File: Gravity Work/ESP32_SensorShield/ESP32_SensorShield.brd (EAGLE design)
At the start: 65.4 x 22.9 mm, 46 parts, among them IC1 BMP388, U1 FGPMMOPA6H, U2 MB85RC256VPF-G-JNERE2, U3 SPX3819-3.3, U4 SN65HVD230D, Y1 32.768kHz

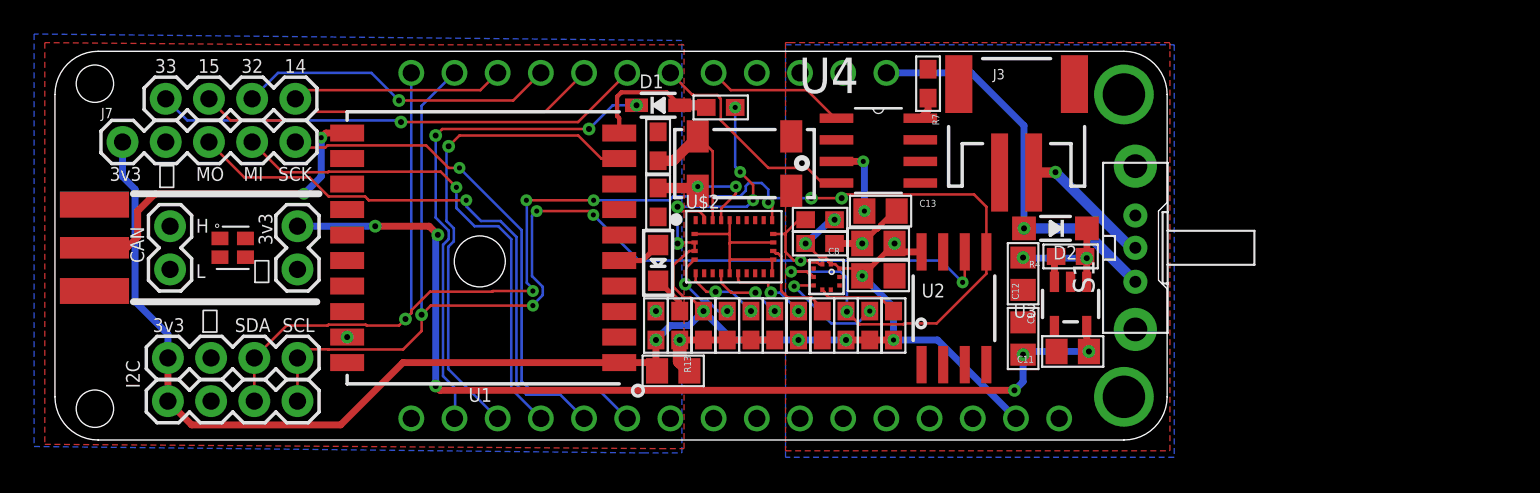
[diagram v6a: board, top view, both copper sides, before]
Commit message: Completed Routing and Fixed DRC Errors. Need to Perfrom Final Check w/ Butch and Selfcheck.
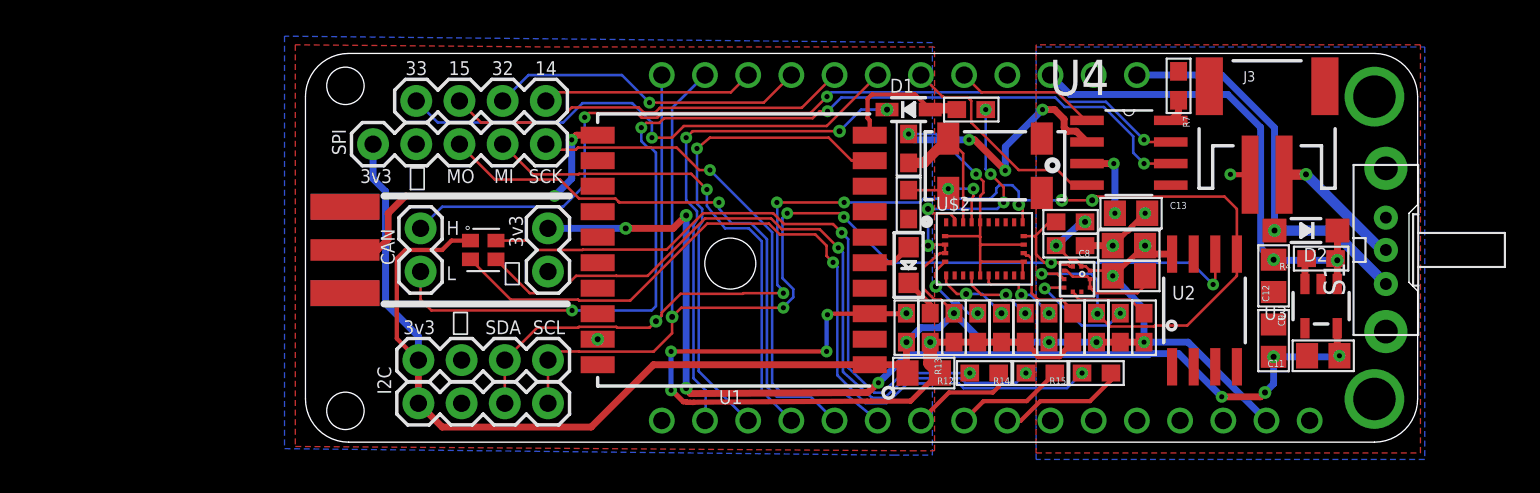
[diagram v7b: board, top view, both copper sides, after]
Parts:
- removed J1, J2, J8: (no value), SparkFun-Connectors:1X04
- removed J4, J6: (no value), SparkFun-Connectors:1X02
- removed J7: (no value), SparkFun-Connectors:1X05
- added AUX_3V3, CAN: (no value), SparkFun-Connectors:1X02
- added CS, I2C1, I2C2: (no value), SparkFun-Connectors:1X04
- added R12, R14, R15: 1k, microbuilder:0603
- added SPI: (no value), SparkFun-Connectors:1X05
- moved D1 14.7 mm to (35.6, 19.6)
- moved C11 14.7 mm to (59.9, 5.08)
- moved C12 14.7 mm to (57.0, 5.97)
- moved C8 14.7 mm to (48.5, 11.6)
- moved C9 14.7 mm to (57.0, 9.78)
- moved J3 14.7 mm to (56.6, 19.4)
- moved U2 14.7 mm to (53.0, 7.75)
- moved U4 14.7 mm to (48.5, 17.0)
- moved C1 14.7 mm to (35.6, 17.3)
- moved C2 14.7 mm to (35.6, 14.0)
- moved LED1 14.7 mm to (35.6, 10.4)
- moved R10 14.7 mm to (39.2, 19.6)
- moved R2 14.7 mm to (39.6, 6.73)
- moved R3 14.7 mm to (45.2, 6.73)
- moved R9 14.7 mm to (46.6, 6.73)
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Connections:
- new net LED_B: R12.1, U$1.10
- new net LED_G: R14.1, U$1.9
- new net LED_R: R15.1, U$1.8
- new net N$12: R12.2, U$36.BLUE
- new net N$13: R14.2, U$36.GREEN
- new net N$14: R15.2, U$36.RED
- net 3.3V: now also I2C1.1, I2C2.1, SPI.1, U$36.CA; no longer J1.1, J2.1, J7.1
- net AUX_3V3: now also AUX_3V3.2; no longer J4.2
- net CANH: now also CAN.2
- net CANL: now also CAN.1
- net GND: now also AUX_3V3.1, I2C1.2, I2C2.2, SPI.2; no longer J1.2, J2.2, J4.1, J7.2
- net GPIO14: now also CS.4; no longer J8.4
- net GPIO15: now also CS.2; no longer J8.2
- net GPIO32: now also CS.3; no longer J8.3
- net GPIO33: now also CS.1; no longer J8.1
- net MISO: now also SPI.4; no longer J7.4
- net MOSI: now also SPI.3; no longer J7.3
- net SCK: now also SPI.5; no longer J7.5
- net SCL: now also I2C1.4, I2C2.4; no longer J1.4, J2.4
- net SDA: now also I2C1.3, I2C2.3; no longer J1.3, J2.3
- net VUSB: now also U$1.19
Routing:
- net GND: track 23.3 -> 92.4 mm, vias 4 -> 15
- net CANL: track 0.00 -> 60.9 mm, vias 0 -> 4
- net CANH: track 0.00 -> 51.2 mm, vias 0 -> 3
- net N$14: track 0.00 -> 48.3 mm, vias 0 -> 2
- net N$13: track 0.00 -> 43.1 mm, vias 0 -> 2
- net N$12: track 0.00 -> 38.2 mm, vias 0 -> 2
- net VUSB: track 6.99 -> 28.8 mm
- net 3.3V: track 110.6 -> 121.7 mm
- net LED_R: track 0.00 -> 7.50 mm
- net LED_G: track 0.00 -> 6.49 mm
- net LED_B: track 0.00 -> 6.20 mm
- net AUX_3V3: track 59.4 -> 62.7 mm, vias 6 -> 8
- net GPIO33: track 28.9 -> 31.0 mm
- net N$2: track 6.97 -> 6.09 mm
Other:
- board text added: "SPI"

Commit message: Added CAN Resistor, GPS GND Line Connected, Fixed Decoup Cap Value for AUX 3V3, Fixed Switch to not extend board size
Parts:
- added R16: 120, microbuilder:0603
- C12: value 0.1uF -> 1uF
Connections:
- removed net GND1: X1.GND@4
- removed net GND2: X1.GND@3
- net CANH: now also R16.1
- net CANL: now also R16.2
- net GND: now also U1.P$12, X1.GND@3, X1.GND@4
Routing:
- net CANH: track 51.2 -> 57.7 mm, vias 3 -> 5
- net CANL: track 60.9 -> 66.0 mm, vias 4 -> 6
- net GND: track 92.4 -> 94.4 mm, vias 15 -> 16
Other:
- board text added: "CS"
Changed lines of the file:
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@@
 <text x="10.668" y="6.35" size="0.8128" layer="25">SDA</text>
 <text x="13.462" y="6.35" size="0.8128" layer="25">SCL</text>
-<text x="5.334" y="10.414" size="0.8128" layer="25" rot="R90">CAN</text>
+<text x="5.334" y="10.033" size="0.8128" layer="25" rot="R90">CAN</text>
 <text x="3.302" y="15.24" size="0.8128" layer="25">3v3</text>
 <text x="8.382" y="15.24" size="0.8128" layer="25">MO</text>
@@
 <text x="8.636" y="6.35" size="1.27" layer="25">⏚</text>
 <text x="1.651" y="18.415" size="0.8128" layer="25" rot="R270">SPI</text>
+<text x="4.191" y="20.955" size="0.8128" layer="25" rot="R270">CS</text>
 </plain>
 <attributes>
@@
 </element>
 <element name="U2" library="microbuilder" package="SOIC8_208MIL" value="MB85RC256VPF-G-JNERE2" x="52.959" y="7.747"/>
-<element name="S1" library="adafruit" library_urn="urn:adsk.eagle:library:420" package="EG1213" value="EG1213" x="63.627" y="11.303" rot="R90"/>
+<element name="S1" library="adafruit" package="EG1213" value="EG1213" x="63.627" y="11.303" rot="R90"/>
 <element name="X1" library="adafruit" package="SMA_EDGELAUNCH" value="" x="0.381" y="11.303" smashed="yes">
 <attribute name="VALUE" x="5.461" y="3.683" size="0.8128" layer="27" ratio="10" rot="R180"/>
@@
 <element name="R4" library="microbuilder" package="0603" value="10K" x="59.817" y="10.795" rot="R180"/>
 <element name="C11" library="microbuilder" package="0805" value="10uF" x="59.944" y="5.08" rot="R180"/>
-<element name="C12" library="microbuilder" package="0805" value="0.1uF" x="57.023" y="5.969" rot="R90"/>
+<element name="C12" library="microbuilder" package="0805" value="1uF" x="57.023" y="5.969" rot="R90"/>
 <element name="I2C1" library="SparkFun-Connectors" library_urn="urn:adsk.eagle:library:513" package="1X04" package3d_urn="urn:adsk.eagle:package:38085/1" value="" x="6.731" y="2.286" smashed="yes">
 <attribute name="PROD_ID" value="CONN-09696" x="6.731" y="2.286" size="1.778" layer="27" display="off"/>
@@
 <attribute name="VALUE" x="5.461" y="2.794" size="0.6096" layer="27" font="vector" ratio="20"/>
 </element>
-<element name="U4" library="SN65HVD230D" package="SOIC127P600X175-8N" value="SN65HVD230D" x="48.514" y="17.018">
+<element name="U4" library="SN65HVD230D" package="SOIC127P600X175-8N" value="SN65HVD230D" x="48.514" y="17.018" smashed="yes">
 <attribute name="AVAILABILITY" value="Unavailable" x="48.514" y="17.018" size="1.778" layer="27" display="off"/>
 <attribute name="DESCRIPTION" value=" 1/1 Transceiver Half CANbus 8-SOIC " x="48.514" y="17.018" size="1.778" layer="27" display="off"/>
 <attribute name="MF" value="Texas Instruments" x="48.514" y="17.018" size="1.778" layer="27" display="off"/>
 <attribute name="MP" value="SN65HVD230D" x="48.514" y="17.018" size="1.778" layer="27" display="off"/>
+<attribute name="NAME" x="43.833290625" y="20.401340625" size="2.08596875" layer="25" ratio="10" rot="SR0"/>
 <attribute name="PACKAGE" value="SOIC-8 Texas Instruments" x="48.514" y="17.018" size="1.778" layer="27" display="off"/>
 <attribute name="PRICE" value="None" x="48.514" y="17.018" size="1.778" layer="27" display="off"/>
@@
 <element name="R14" library="microbuilder" package="0603" value="1k" x="43.307" y="4.064" rot="R180"/>
 <element name="R15" library="microbuilder" package="0603" value="1k" x="46.609" y="4.064" rot="R180"/>
+<element name="R16" library="microbuilder" package="0603" value="120" x="52.324" y="13.335" rot="R180"/>
 </elements>
 <signals>
@@
 <wire x1="54.5" y1="15.731" x2="54.483" y2="15.748" width="0.3048" layer="1"/>
 <via x="54.483" y="15.748" extent="1-16" drill="0.3"/>
+<contactref element="U1" pad="P$12"/>
+<contactref element="X1" pad="GND@4"/>
+<contactref element="X1" pad="GND@3"/>
+<wire x1="17.273" y1="16.553" x2="19.261" y2="16.553" width="0.4064" layer="1"/>
+<wire x1="19.261" y1="16.553" x2="19.304" y2="16.51" width="0.4064" layer="1"/>
+<via x="19.304" y="16.51" extent="1-16" drill="0.3"/>
 </signal>
 <signal name="3.3V">
@@
 <wire x1="34.649" y1="10.553" x2="35.56" y2="11.464" width="0.3048" layer="1"/>
 </signal>
-<signal name="GND1">
-<contactref element="X1" pad="GND@4"/>
-</signal>
-<signal name="GND2">
-<contactref element="X1" pad="GND@3"/>
-</signal>
 <signal name="N$6">
 <contactref element="J3" pad="2"/>
@@
 <wire x1="6.858" y1="8.382" x2="6.858" y2="10.033" width="0.1524" layer="1"/>
 <wire x1="7.493" y1="7.747" x2="6.858" y2="8.382" width="0.1524" layer="1"/>
+<contactref element="R16" pad="2"/>
+<via x="51.474" y="13.335" extent="1-16" drill="0.3"/>
+<wire x1="51.474" y1="13.335" x2="52.578" y2="14.439" width="0.1524" layer="16"/>
+<wire x1="52.578" y1="14.439" x2="52.578" y2="16.383" width="0.1524" layer="16"/>
+<via x="52.578" y="16.383" extent="1-16" drill="0.3"/>
+<wire x1="52.578" y1="16.383" x2="50.9778" y2="16.383" width="0.1524" layer="1"/>
 </signal>
 <signal name="CANH">
@@
 <wire x1="16.51" y1="15.113" x2="15.24" y2="13.843" width="0.1524" layer="16"/>
 <wire x1="15.24" y1="13.843" x2="8.128" y2="13.843" width="0.1524" layer="16"/>
+<contactref element="R16" pad="1"/>
+<wire x1="50.9778" y1="17.653" x2="53.086" y2="17.653" width="0.1524" layer="1"/>
+<wire x1="53.086" y1="17.653" x2="53.213" y2="17.526" width="0.1524" layer="1"/>
+<via x="53.213" y="17.526" extent="1-16" drill="0.3"/>
+<wire x1="53.213" y1="17.526" x2="53.213" y2="13.374" width="0.1524" layer="16"/>
+<wire x1="53.213" y1="13.374" x2="53.174" y2="13.335" width="0.1524" layer="16"/>
+<via x="53.174" y="13.335" extent="1-16" drill="0.3"/>
 </signal>
 <signal name="N$10">
